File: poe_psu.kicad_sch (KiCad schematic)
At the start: 40 parts

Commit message: finish shcematic
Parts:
- removed L?: UPZ2012E601-2R0TF, symbol Device:L
- removed U?: EL3H7, symbol Isolator:EL817
- added D6: 12V, symbol Device:D_TVS
- added L5: UPZ2012E601-2R0TF, Inductor_SMD:L_0805_2012Metric_Pad1.15x1.40mm_HandSolder, symbol Device:L
- added U3: EL3H7-G, project specific:SOIC127P700X200-4N, symbol EL3H7-G:EL3H7-G
- C24: renamed from C?; value 22pF -> 220pF
- D5: renamed from D?; footprint (none) -> Diode_SMD:D_SMA_Handsoldering; LCSC (none) -> C513478
- L4: renamed from L?; footprint (none) -> Inductor_SMD:L_0805_2012Metric_Pad1.15x1.40mm_HandSolder; LCSC (none) -> C98308
- T1: renamed from T?; footprint (none) -> project specific:HR051142; LCSC (none) -> C55680
- U2: renamed from U?; footprint QFN50P400X400X90-21N -> project specific:QFN50P400X400X90-21N
- gave numbers to parts that had none: 33
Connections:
- net +12V: now also D6.2 (A2)
- net GND: now also D6.1 (A1), L5.2
- net VSS: now also U3.3
- net at C25.1, C26.1, D5.1 (K)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: now also C24.2
- net at C20.2, C25.2, C26.2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: now also L5.1
- net at R17.2: now also U3.1
- net at C21.1, U4.1 (K): now also U3.2
- net at R13.2, R15.1, U2.3 (EROUT): now also U3.4
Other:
- moved on the sheet: C21, C22, C23, R17, R18, R20, R21, U4

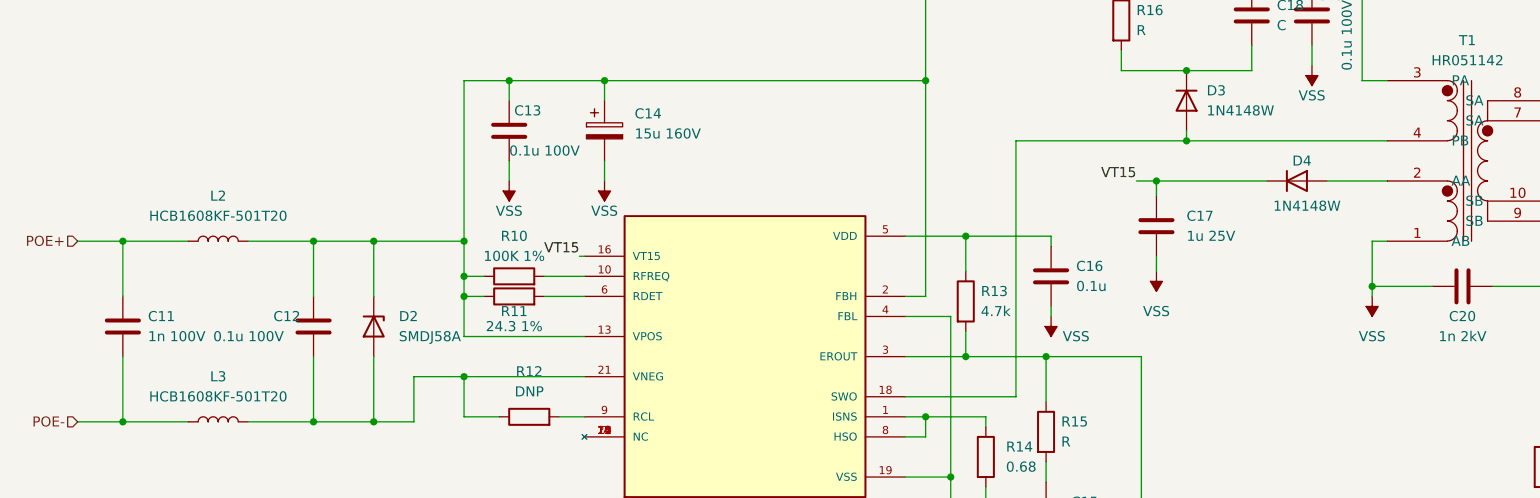
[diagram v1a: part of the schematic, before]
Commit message: feat: add more LCSC symbols
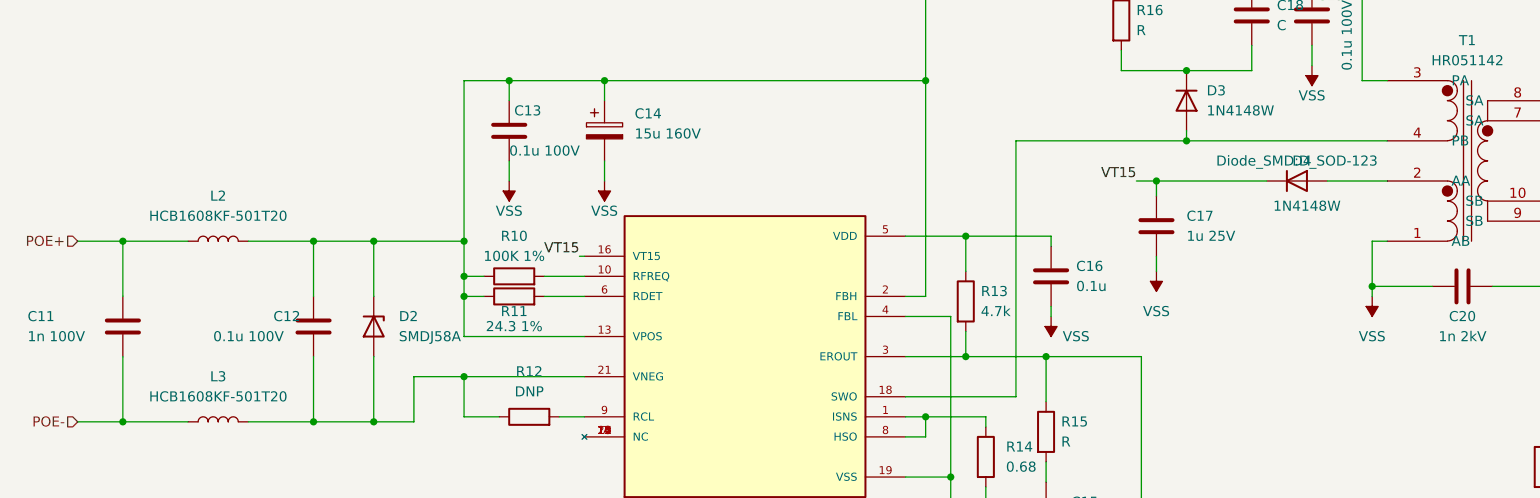
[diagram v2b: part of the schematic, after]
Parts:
- C20: footprint (none) -> Capacitor_SMD:C_1206_3216Metric_Pad1.33x1.80mm_HandSolder; LCSC (none) -> C363565
- D2: footprint (none) -> Diode_SMD:D_SMB-SMC_Universal_Handsoldering; LCSC (none) -> C4154735
- D3: footprint (none) -> Diode_SMD:D_SOD-123; LCSC (none) -> C444720
- D4: footprint (none) -> Diode_SMD:D_SOD-123; LCSC (none) -> C181133
- L2: footprint (none) -> Inductor_SMD:L_0603_1608Metric; LCSC (none) -> C356979
- L3: footprint (none) -> Inductor_SMD:L_0603_1608Metric
- R20: footprint (none) -> Resistor_SMD:R_0603_1608Metric_Pad0.98x0.95mm_HandSolder; LCSC (none) -> C137719
- R21: footprint (none) -> Resistor_SMD:R_0603_1608Metric_Pad0.98x0.95mm_HandSolder; LCSC (none) -> C137803
- U2: LCSC (none) -> C461934
- U3: LCSC (none) -> C92243
- U4: LCSC (none) -> C97717
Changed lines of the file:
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@@
     (property "Reference" "L2" (id 0) (at 43.815 75.565 90))
     (property "Value" "HCB1608KF-501T20" (id 1) (at 43.815 78.105 90))
-    (property "Footprint" "" (id 2) (at 43.815 81.28 0)
-      (effects (font (size 1.27 1.27)) hide)
-    )
-    (property "Datasheet" "~" (id 3) (at 43.815 81.28 0)
+    (property "Footprint" "Inductor_SMD:L_0603_1608Metric" (id 2) (at 43.815 81.28 0)
+      (effects (font (size 1.27 1.27)) hide)
+    )
+    (property "Datasheet" "https://datasheet.lcsc.com/lcsc/2009171138_TAI-TECH-HCB1608KF-501T20_C356979.pdf" (id 3) (at 43.815 81.28 0)
+      (effects (font (size 1.27 1.27)) hide)
+    )
+    (property "LCSC" "C356979" (id 4) (at 43.815 81.28 90)
       (effects (font (size 1.27 1.27)) hide)
     )
@@
   )
   (symbol (lib_id "Device:C") (at 31.75 92.075 0) (unit 1)
-    (in_bom yes) (on_board yes) (fields_autoplaced)
-    (property "Reference" "C11" (id 0) (at 34.925 90.8049 0)
-      (effects (font (size 1.27 1.27)) (justify left))
-    )
-    (property "Value" "1n 100V" (id 1) (at 34.925 93.3449 0)
+    (in_bom yes) (on_board yes)
+    (property "Reference" "C11" (id 0) (at 19.685 90.805 0)
+      (effects (font (size 1.27 1.27)) (justify left))
+    )
+    (property "Value" "1n 100V" (id 1) (at 19.685 93.345 0)
       (effects (font (size 1.27 1.27)) (justify left))
     )
@@
       (effects (font (size 1.27 1.27)) (justify left))
     )
-    (property "Footprint" "" (id 2) (at 166.37 63.5 0)
-      (effects (font (size 1.27 1.27)) hide)
-    )
-    (property "Datasheet" "~" (id 3) (at 166.37 63.5 0)
+    (property "Footprint" "Diode_SMD:D_SOD-123" (id 2) (at 166.37 63.5 0)
+      (effects (font (size 1.27 1.27)) hide)
+    )
+    (property "Datasheet" "https://datasheet.lcsc.com/lcsc/1912111437_Slkor-SLKORMICRO-Elec--1N4148W_C444720.pdf" (id 3) (at 166.37 63.5 0)
+      (effects (font (size 1.27 1.27)) hide)
+    )
+    (property "LCSC" "C444720" (id 4) (at 166.37 63.5 90)
       (effects (font (size 1.27 1.27)) hide)
     )
@@
       (effects (font (size 1.27 1.27)) (justify left bottom) hide)
     )
-    (property "Datasheet" "" (id 3) (at 187.96 127.635 0)
+    (property "Datasheet" "https://datasheet.lcsc.com/lcsc/1811091923_Everlight-Elec-EL3H7-C-TA-G_C92243.pdf" (id 3) (at 187.96 127.635 0)
       (effects (font (size 1.27 1.27)) (justify left bottom) hide)
     )
@@
     (property "PARTREV" "7" (id 7) (at 187.96 127.635 0)
       (effects (font (size 1.27 1.27)) (justify left bottom) hide)
+    )
+    (property "LCSC" "C92243" (id 8) (at 187.96 127.635 0)
+      (effects (font (size 1.27 1.27)) hide)
     )
     (pin "1")
@@
       (effects (font (size 1.27 1.27)) (justify left bottom) hide)
     )
-    (property "Datasheet" "" (id 3) (at 110.49 95.885 0)
+    (property "Datasheet" "https://datasheet.lcsc.com/lcsc/2108241830_SILICON-LABS-SI3404-A-GMR_C461934.pdf" (id 3) (at 110.49 95.885 0)
       (effects (font (size 1.27 1.27)) (justify left bottom) hide)
     )
@@
     (property "MANUFACTURER" "Silicon Labs" (id 40) (at 110.49 95.885 0)
       (effects (font (size 1.27 1.27)) (justify left bottom) hide)
+    )
+    (property "LCSC" "C461934" (id 41) (at 110.49 95.885 0)
+      (effects (font (size 1.27 1.27)) hide)
     )
     (pin "1")
@@
       (effects (font (size 1.27 1.27)) (justify left))
     )
-    (property "Footprint" "" (id 2) (at 255.397 121.92 90)
-      (effects (font (size 1.27 1.27)) hide)
-    )
-    (property "Datasheet" "~" (id 3) (at 257.175 121.92 0)
+    (property "Footprint" "Resistor_SMD:R_0603_1608Metric_Pad0.98x0.95mm_HandSolder" (id 2) (at 255.397 121.92 90)
+      (effects (font (size 1.27 1.27)) hide)
+    )
+    (property "Datasheet" "https://datasheet.lcsc.com/lcsc/1811082114_YAGEO-RC0603FR-0743KL_C137719.pdf" (id 3) (at 257.175 121.92 0)
+      (effects (font (size 1.27 1.27)) hide)
+    )
+    (property "LCSC" "C137719" (id 4) (at 257.175 121.92 0)
       (effects (font (size 1.27 1.27)) hide)
     )
@@
     (property "Reference" "L3" (id 0) (at 43.815 98.425 90))
     (property "Value" "HCB1608KF-501T20" (id 1) (at 43.815 100.965 90))
-    (property "Footprint" "" (id 2) (at 43.815 104.14 0)
+    (property "Footprint" "Inductor_SMD:L_0603_1608Metric" (id 2) (at 43.815 104.14 0)
       (effects (font (size 1.27 1.27)) hide)
     )
@@
     (property "Reference" "D4" (id 0) (at 180.975 71.12 0))
     (property "Value" "1N4148W" (id 1) (at 181.61 76.835 0))
-    (property "Footprint" "" (id 2) (at 180.34 73.66 0)
-      (effects (font (size 1.27 1.27)) hide)
-    )
-    (property "Datasheet" "~" (id 3) (at 180.34 73.66 0)
+    (property "Footprint" "Diode_SMD:D_SOD-123" (id 2) (at 180.34 71.12 0))
+    (property "Datasheet" "https://datasheet.lcsc.com/lcsc/1809291522_Guangdong-Hottech-1N4148WS_C181133.pdf" (id 3) (at 180.34 73.66 0)
+      (effects (font (size 1.27 1.27)) hide)
+    )
+    (property "LCSC" "C181133" (id 4) (at 180.34 73.66 0)
       (effects (font (size 1.27 1.27)) hide)
     )
@@
       (effects (font (size 1.27 1.27)) (justify left))
     )
-    (property "Footprint" "" (id 2) (at 63.5 92.075 0)
-      (effects (font (size 1.27 1.27)) hide)
-    )
-    (property "Datasheet" "~" (id 3) (at 63.5 92.075 0)
+    (property "Footprint" "Diode_SMD:D_SMB-SMC_Universal_Handsoldering" (id 2) (at 63.5 92.075 0)
+      (effects (font (size 1.27 1.27)) hide)
+    )
+    (property "Datasheet" "https://datasheet.lcsc.com/lcsc/2209291730_TWGMC-SMDJ58A_C4154735.pdf" (id 3) (at 63.5 92.075 0)
+      (effects (font (size 1.27 1.27)) hide)
+    )
+    (property "LCSC" "C4154735" (id 4) (at 63.5 92.075 90)
       (effects (font (size 1.27 1.27)) hide)
     )
@@
       (effects (font (size 1.27 1.27)) (justify left))
     )
-    (property "Footprint" "" (id 2) (at 255.397 137.795 90)
-      (effects (font (size 1.27 1.27)) hide)
-    )
-    (property "Datasheet" "~" (id 3) (at 257.175 137.795 0)
+    (property "Footprint" "Resistor_SMD:R_0603_1608Metric_Pad0.98x0.95mm_HandSolder" (id 2) (at 255.397 137.795 90)
+      (effects (font (size 1.27 1.27)) hide)
+    )
+    (property "Datasheet" "https://datasheet.lcsc.com/lcsc/1811082124_YAGEO-RC0603FR-0711K3L_C137803.pdf" (id 3) (at 257.175 137.795 0)
+      (effects (font (size 1.27 1.27)) hide)
+    )
+    (property "LCSC" "C137803" (id 4) (at 257.175 137.795 0)
       (effects (font (size 1.27 1.27)) hide)
     )
@@
     )
     (property "Datasheet" "https://www.diodes.com/assets/Datasheets/AN431.pdf" (id 3) (at 208.915 142.24 0)
+      (effects (font (size 1.27 1.27)) hide)
+    )
+    (property "LCSC" "C97717" (id 4) (at 208.915 142.24 90)
       (effects (font (size 1.27 1.27)) hide)
     )
@@
     (property "Reference" "C20" (id 0) (at 201.295 90.805 90))
     (property "Value" "1n 2kV" (id 1) (at 201.295 93.345 90))
-    (property "Footprint" "" (id 2) (at 205.105 86.0298 0)
-      (effects (font (size 1.27 1.27)) hide)
-    )
-    (property "Datasheet" "~" (id 3) (at 201.295 86.995 0)
-      (effects (font (size 1.27 1.27)) hide)
-    )
+    (property "Footprint" "Capacitor_SMD:C_1206_3216Metric_Pad1.33x1.80mm_HandSolder" (id 2) (at 205.105 86.0298 0)
+      (effects (font (size 1.27 1.27)) hide)
+    )
+    (property "Datasheet" "https://datasheet.lcsc.com/lcsc/1912111437_PSA-Prosperity-Dielectrics-FV31X102K202PXG_C363565.pdf" (id 3) (at 201.295 86.995 0)
+      (effects (font (size 1.27 1.27)) hide)
+    )
+    (property "LCSC" "C363565" (id 4) (at 201.295 86.995 90)
+      (effects (font (size 1.27 1.27)) hide)
+    )

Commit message: Add some more footprints
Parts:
- C11, C12, C13, C14, C15, C16, C17, C18, C19: footprint (none) -> Capacitor_SMD:C_0603_1608Metric_Pad1.08x0.95mm_HandSolder
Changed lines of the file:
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@@
       (effects (font (size 1.27 1.27)) (justify left))
     )
-    (property "Footprint" "" (id 2) (at 150.1902 89.535 0)
+    (property "Footprint" "Capacitor_SMD:C_0603_1608Metric_Pad1.08x0.95mm_HandSolder" (id 2) (at 150.1902 89.535 0)
       (effects (font (size 1.27 1.27)) hide)
     )
@@
       (effects (font (size 1.27 1.27)) (justify left))
     )
-    (property "Footprint" "" (id 2) (at 163.5252 83.185 0)
+    (property "Footprint" "Capacitor_SMD:C_0603_1608Metric_Pad1.08x0.95mm_HandSolder" (id 2) (at 163.5252 83.185 0)
       (effects (font (size 1.27 1.27)) hide)
     )
@@
       (effects (font (size 1.27 1.27)) (justify left))
     )
-    (property "Footprint" "" (id 2) (at 93.6752 71.12 0)
+    (property "Footprint" "Capacitor_SMD:C_0603_1608Metric_Pad1.08x0.95mm_HandSolder" (id 2) (at 93.6752 71.12 0)
       (effects (font (size 1.27 1.27)) hide)
     )
@@
       (effects (font (size 1.27 1.27)) (justify left))
     )
-    (property "Footprint" "" (id 2) (at 32.7152 95.885 0)
+    (property "Footprint" "Capacitor_SMD:C_0603_1608Metric_Pad1.08x0.95mm_HandSolder" (id 2) (at 32.7152 95.885 0)
       (effects (font (size 1.27 1.27)) hide)
     )
@@
       (effects (font (size 1.27 1.27)) (justify left))
     )
-    (property "Footprint" "" (id 2) (at 56.8452 95.885 0)
+    (property "Footprint" "Capacitor_SMD:C_0603_1608Metric_Pad1.08x0.95mm_HandSolder" (id 2) (at 56.8452 95.885 0)
       (effects (font (size 1.27 1.27)) hide)
     )
@@
       (effects (font (size 1.27 1.27)) (justify left))
     )
-    (property "Footprint" "" (id 2) (at 149.5552 119.38 0)
+    (property "Footprint" "Capacitor_SMD:C_0603_1608Metric_Pad1.08x0.95mm_HandSolder" (id 2) (at 149.5552 119.38 0)
       (effects (font (size 1.27 1.27)) hide)
     )
@@
       (effects (font (size 1.27 1.27)) (justify left))
     )
-    (property "Footprint" "" (id 2) (at 175.5902 56.515 0)
+    (property "Footprint" "Capacitor_SMD:C_0603_1608Metric_Pad1.08x0.95mm_HandSolder" (id 2) (at 175.5902 56.515 0)
       (effects (font (size 1.27 1.27)) hide)
     )
@@
       (effects (font (size 1.27 1.27)) (justify left))
     )
-    (property "Footprint" "" (id 2) (at 81.6102 71.12 0)
+    (property "Footprint" "Capacitor_SMD:C_0603_1608Metric_Pad1.08x0.95mm_HandSolder" (id 2) (at 81.6102 71.12 0)
       (effects (font (size 1.27 1.27)) hide)
     )
@@
       (effects (font (size 1.27 1.27)) (justify left))
     )
-    (property "Footprint" "" (id 2) (at 183.2102 56.515 0)
-      (effects (font (size 1.27 1.27)) hide)
-    )
+    (property "Footprint" "Capacitor_SMD:C_0603_1608Metric_Pad1.08x0.95mm_HandSolder" (id 2) (at 183.2102 56.515 0)
+      (effects (font (size 1.27 1.27)) hide)
+    )
